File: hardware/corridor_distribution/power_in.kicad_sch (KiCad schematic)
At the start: 14 parts, among them J9 Screw_Terminal_01x02, U1 TD1465

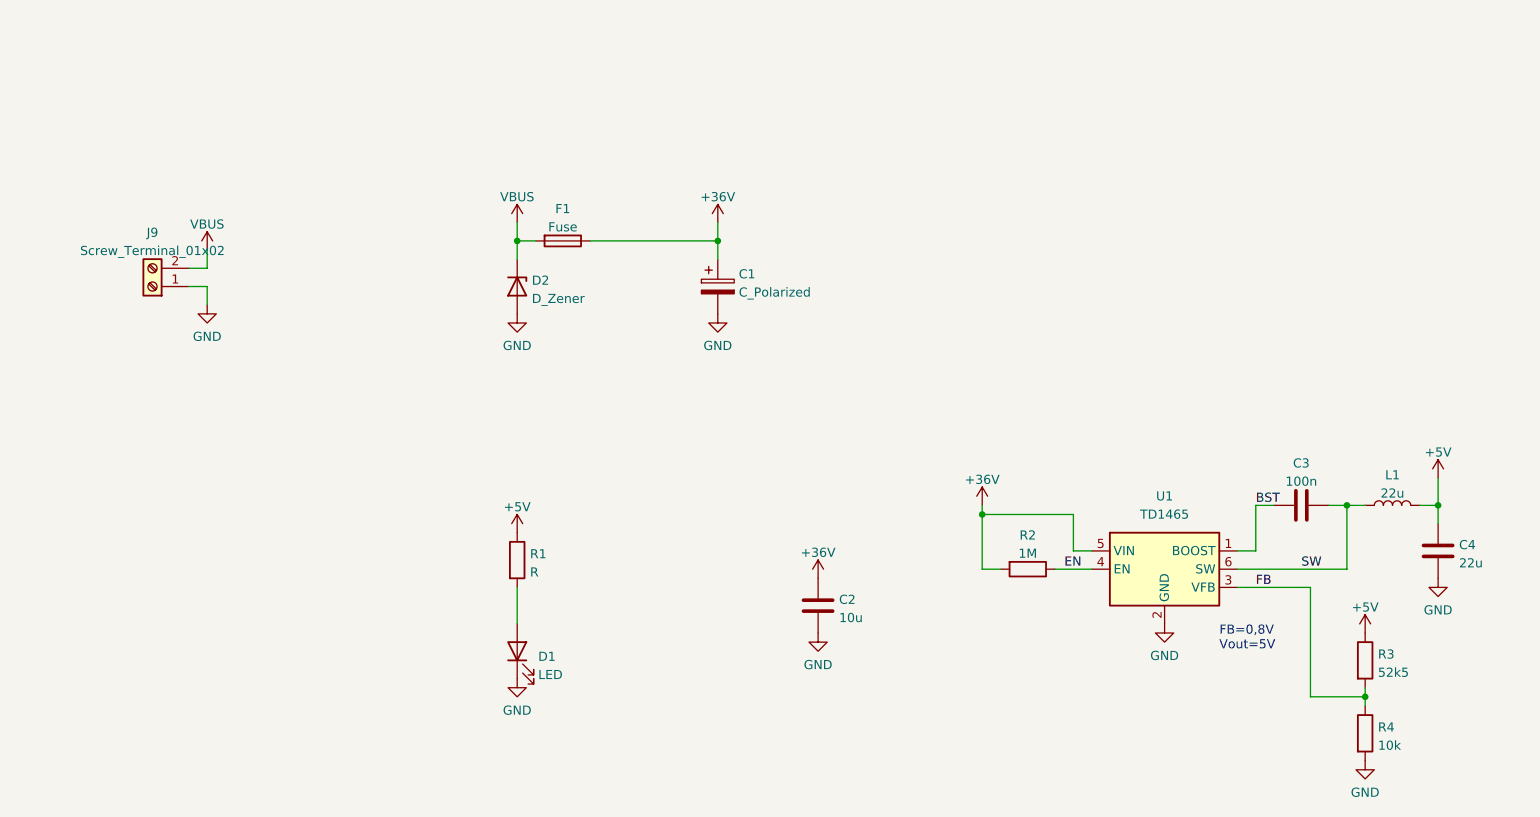
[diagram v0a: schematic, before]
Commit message: led balance and corridor ready
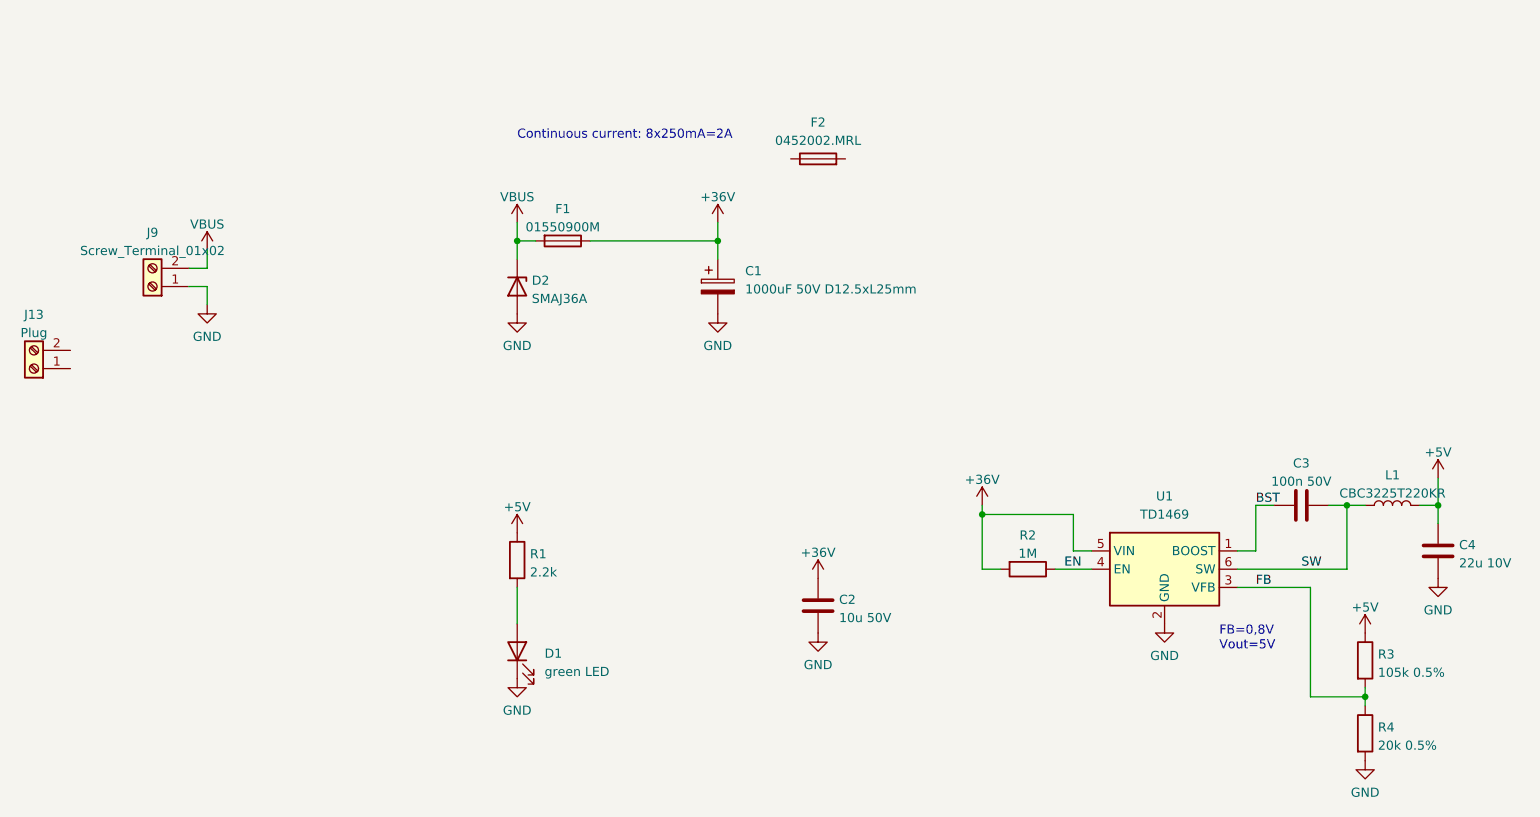
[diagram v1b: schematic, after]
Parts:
- added F2: 0452002.MRL, symbol Device:Fuse
- added J13: Plug, Connector_Phoenix_MSTB:PhoenixContact_MSTBVA_2,5_2-G_1x02_P5.00mm_Vertical, symbol Connector:Screw_Terminal_01x02
- C1: value C_Polarized -> 1000uF 50V D12.5xL25mm; LCSC Part # (none) -> C338226; Total quantity (none) -> 5
- C2: value 10u -> 10u 50V; footprint Capacitor_SMD:C_1206_3216Metric -> Capacitor_SMD:C_1210_3225Metric; LCSC Part # (none) -> C337485; Total quantity (none) -> 50
- C3: value 100n -> 100n 50V; LCSC Part # (none) -> C14663; Total quantity (none) -> 30
- C4: value 22u -> 22u 10V; LCSC Part # (none) -> C29277; Total quantity (none) -> 50
- D1: value LED -> green LED
- D2: value D_Zener -> SMAJ36A; LCSC Part # (none) -> C148232; Total quantity (none) -> 5
- F1: value Fuse -> 01550900M; LCSC Part # (none) -> C108518; Total quantity (none) -> 5
- J9: LCSC Part # (none) -> C505779; Total quantity (none) -> 5
- L1: value 22u -> CBC3225T220KR; LCSC Part # (none) -> C223225; Total quantity (none) -> 5
- R1: value R -> 2.2k; LCSC Part # (none) -> C125931; Total quantity (none) -> 5
- R2: LCSC Part # (none) -> C105578; Total quantity (none) -> 5
- R3: value 52k5 -> 105k 0.5%; LCSC Part # (none) -> C862523; Total quantity (none) -> 5
- R4: value 10k -> 20k 0.5%; LCSC Part # (none) -> C227463; Total quantity (none) -> 10
- U1: value TD1465 -> TD1469; LCSC Part # (none) -> C2832208; Total quantity (none) -> 50
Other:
- note added: "Continuous current: 8x250mA=2A"

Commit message: various
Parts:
- added C5: 100n 50V, Capacitor_SMD:C_0603_1608Metric, symbol Device:C
- added R16: R, Resistor_SMD:R_1210_3225Metric_Pad1.30x2.65mm_HandSolder, symbol Device:R
- added U9: INA190, Package_TO_SOT_SMD:SOT-363_SC-70-6, symbol Amplifier_Current:INA199xxDCK
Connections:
- net +36V: now also R16.2, U9.5 (-); no longer F1.1
- net +5V: now also C5.1, U9.3 (V+)
- net GND: now also C5.2, U9.1 (REF), U9.2 (GND)
- new net: F1.1, R16.1, U9.4 (+)
- new net CS: U9.6
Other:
- note added: "Imax = 2A Rs = V/(I*G) |Code |Gain |Rs |Pd | |A1 |25 |100mR |400mW | |A2 |50 |50mR |200mW | |A3 |100 |25mR |100mW | |A4 |200 |12,5mR |50mW | |A5 |500 |5mR |20mW |"
- moved on the sheet: F2

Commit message: Night Light firmware
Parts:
- renumbered C5 to C14
